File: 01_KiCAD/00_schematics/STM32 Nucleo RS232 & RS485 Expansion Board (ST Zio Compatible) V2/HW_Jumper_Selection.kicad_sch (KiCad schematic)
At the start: 0 parts

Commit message: Added components and change device
Added dual Schmidt trigger input SN74LVC2G14DBV for LED Rx and Tx control.
Changed sn74hcs245 for alternate part sn74lvc245a for larger footprint and better availability with LCSC.
Difference is sn74lvc245a has no Schmidt-trigger inputs but instead just normal inputs. Fot details see dataseet. Both devices use exact same pin number and configuration except sn74lvc245a has no thermal pad or exposed pad like the sn74hcs245 has.
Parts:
- added C27: 100nF, PCM_SparkFun-Capacitor:C_0603_1608Metric, symbol PCM_SparkFun-Capacitor:0.1uF_0603_25V_20%
- added D8, D9: LED, IN-S63AT:LED_0603_WRE, symbol PCM_SparkFun-LED:LED
- added J7: DIR, symbol Connector_Generic:Conn_01x03
- added R38: 590R, PCM_fab:R_0603, symbol PCM_fab:R_0603
- added R39: 137R, PCM_fab:R_0603, symbol PCM_fab:R_0603
- added R40, R41: 10K, PCM_fab:R_0603, symbol PCM_fab:R_0603
- added R42: 100K, PCM_fab:R_0603, symbol PCM_fab:R_0603
- added R43: 1M, PCM_fab:R_0603, symbol PCM_fab:R_0603
- added U5: SN74LVC2G14DBV, Package_TO_SOT_SMD:SOT-23-6, symbol 74xGxx:SN74LVC2G14DBV
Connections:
- new net: D8.2 (A), R39.1
- new net: D9.2 (A), R38.2
- new net: J7.1 (Pin_1), R40.2
- new net: J7.3 (Pin_3), R41.2
- new net: R42.2, U5.1 (1A)
- new net: D8.1 (K), U5.3 (2A), U5.6 (1Y)
- new net: D9.1 (K), U5.4 (2Y)
- new net 3V3_SYS: C27.1, R38.1, R39.2, R41.1, R43.2, U5.5 (V_{CC})
- new net DIR: J7.2 (Pin_2), R42.1, R43.1
- new net GND: C27.2, R40.1, U5.2 (GND)

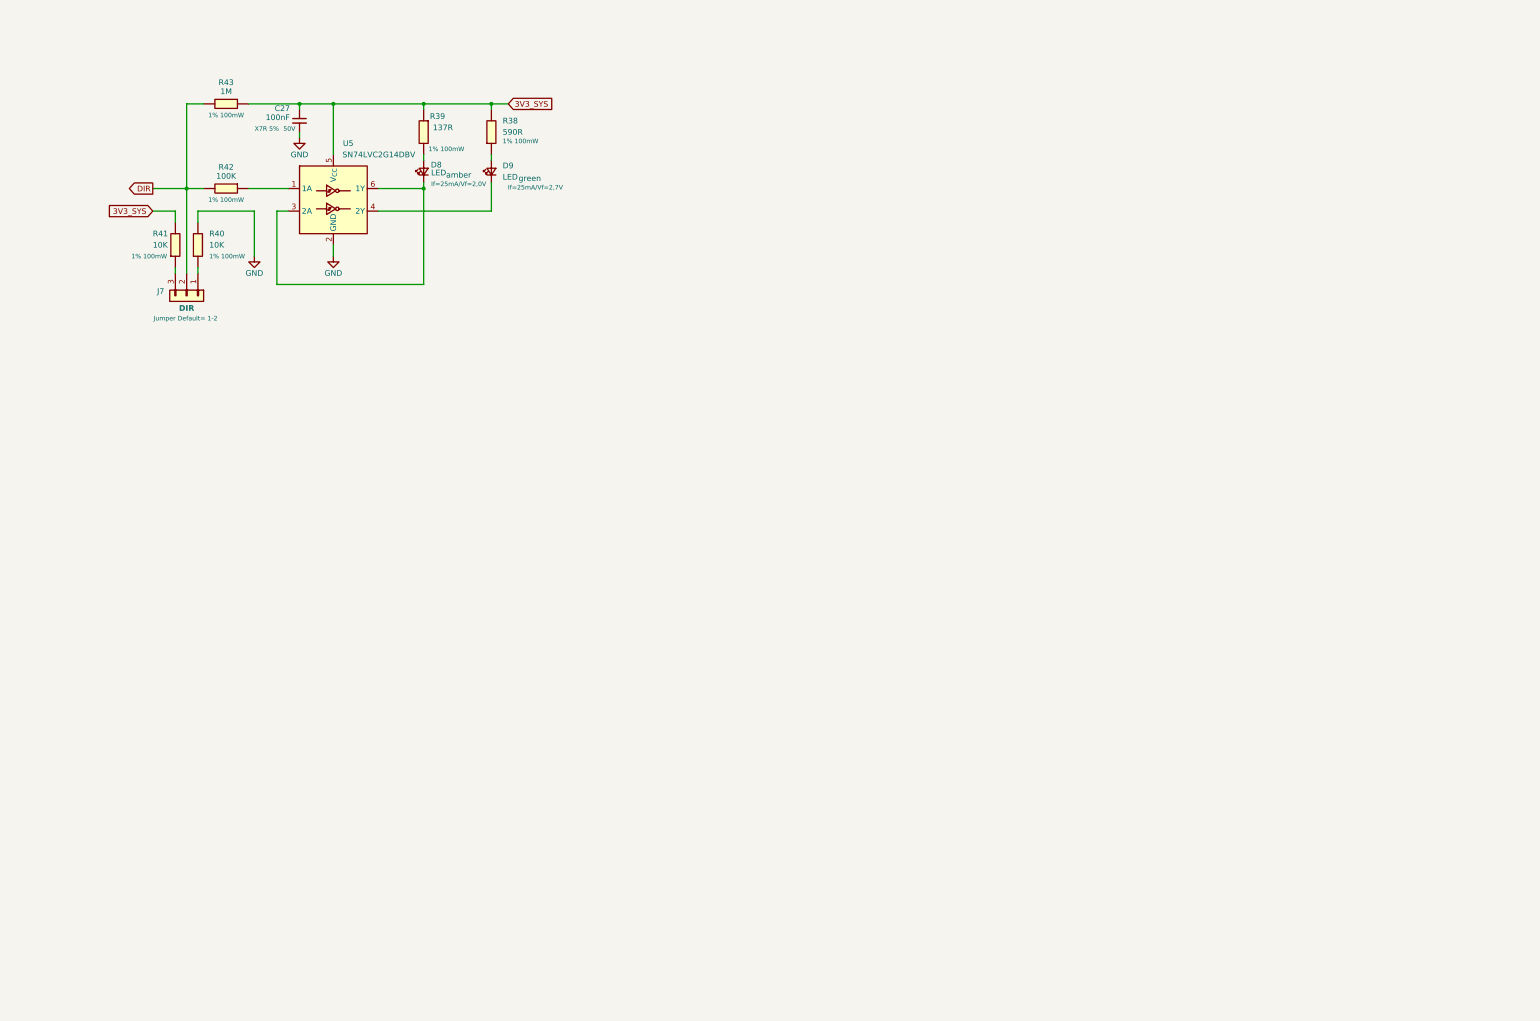
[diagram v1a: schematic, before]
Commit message: Finisching touches to schematics
Finalizing the schematics and double-check all connections throughout the different sheets.
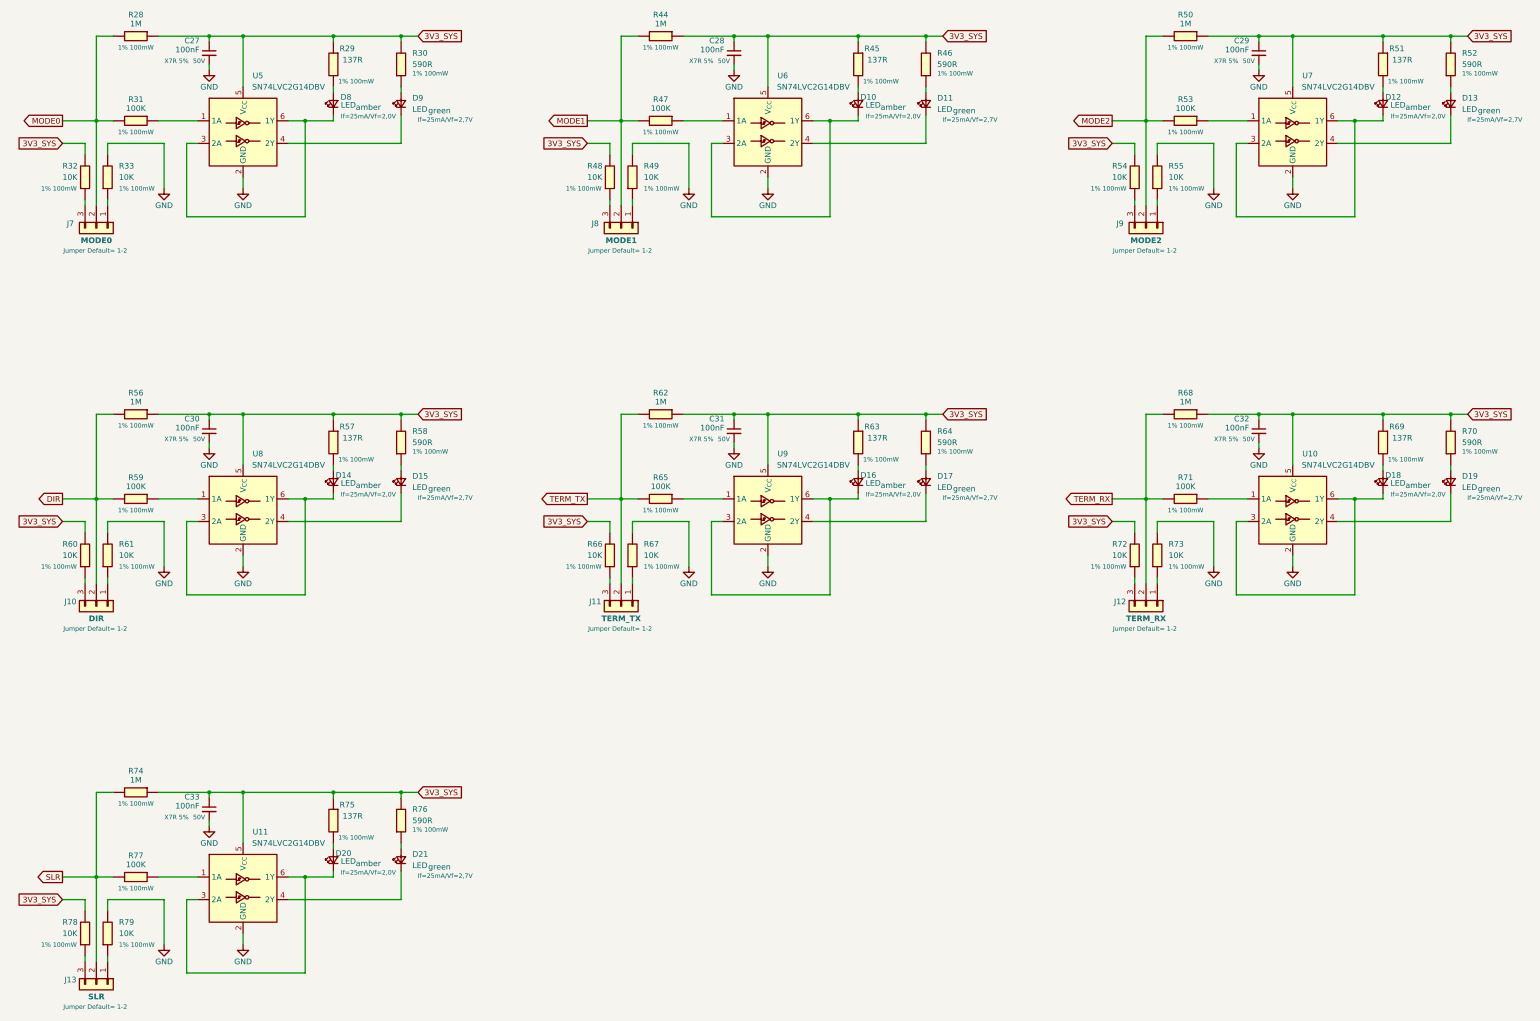
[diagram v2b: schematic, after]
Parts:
- added C28, C29, C30, C31, C32, C33: 100nF, PCM_SparkFun-Capacitor:C_0603_1608Metric, symbol PCM_SparkFun-Capacitor:0.1uF_0603_25V_20%
- added D10, D11, D12, D13, D14, D15, D16, D17, D18, D19, D20, D21: LED, IN-S63AT:LED_0603_WRE, symbol PCM_SparkFun-LED:LED
- added J10: DIR, symbol Connector_Generic:Conn_01x03
- added J11: TERM_TX, symbol Connector_Generic:Conn_01x03
- added J12: TERM_RX, symbol Connector_Generic:Conn_01x03
- added J13: SLR, symbol Connector_Generic:Conn_01x03
- added J8: MODE1, symbol Connector_Generic:Conn_01x03
- added J9: MODE2, symbol Connector_Generic:Conn_01x03
- added R44, R50, R56, R62, R68, R74: 1M, PCM_fab:R_0603, symbol PCM_fab:R_0603
- added R45, R51, R57, R63, R69, R75: 137R, PCM_fab:R_0603, symbol PCM_fab:R_0603
- added R46, R52, R58, R64, R70, R76: 590R, PCM_fab:R_0603, symbol PCM_fab:R_0603
- added R47, R53, R59, R65, R71, R77: 100K, PCM_fab:R_0603, symbol PCM_fab:R_0603
- added R48, R49, R54, R55, R60, R61, R66, R67, R72, R73, R78, R79: 10K, PCM_fab:R_0603, symbol PCM_fab:R_0603
- added U10, U11, U6, U7, U8, U9: SN74LVC2G14DBV, Package_TO_SOT_SMD:SOT-23-6, symbol 74xGxx:SN74LVC2G14DBV
- J7: value DIR -> MODE0
- renumbered R43 to R28, R39 to R29, R38 to R30, R42 to R31, R41 to R32, R40 to R33
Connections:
- net 3V3_SYS: now also C28.1, C29.1, C30.1, C31.1, C32.1, C33.1, R44.2, R45.2, R46.1, R48.1, R50.2, R51.2, R52.1, R54.1, R56.2, R57.2, R58.1, R60.1, R62.2, R63.2, R64.1, R66.1, R68.2, R69.2, R70.1, R72.1, R74.2, R75.2, R76.1, R78.1, U10.5 (V_{CC}), U11.5 (V_{CC}), U6.5 (V_{CC}), U7.5 (V_{CC}), U8.5 (V_{CC}), U9.5 (V_{CC})
- net DIR: now also J10.2 (Pin_2), R56.1, R59.1; no longer J7.2 (Pin_2), R28.1, R31.1
- net GND: now also C28.2, C29.2, C30.2, C31.2, C32.2, C33.2, R49.1, R55.1, R61.1, R67.1, R73.1, R79.1, U10.2 (GND), U11.2 (GND), U6.2 (GND), U7.2 (GND), U8.2 (GND), U9.2 (GND)
- new net: R59.2, U8.1 (1A)
- new net: D14.1 (K), U8.3 (2A), U8.6 (1Y)
- new net: D15.1 (K), U8.4 (2Y)
- new net: D13.2 (A), R52.2
- new net: J13.1 (Pin_1), R79.2
- new net: J10.3 (Pin_3), R60.2
- new net: J9.1 (Pin_1), R55.2
- new net: J9.3 (Pin_3), R54.2
- new net: J12.3 (Pin_3), R72.2
- new net: D21.2 (A), R76.2
- new net: R53.2, U7.1 (1A)
- new net: D12.1 (K), U7.3 (2A), U7.6 (1Y)
- new net: D13.1 (K), U7.4 (2Y)
- new net: D15.2 (A), R58.2
- new net: J11.1 (Pin_1), R67.2
- new net: J10.1 (Pin_1), R61.2
- new net: J11.3 (Pin_3), R66.2
- new net: R47.2, U6.1 (1A)
- new net: R77.2, U11.1 (1A)
- new net: D20.1 (K), U11.3 (2A), U11.6 (1Y)
- new net: D21.1 (K), U11.4 (2Y)
- new net: J8.1 (Pin_1), R49.2
- new net: J8.3 (Pin_3), R48.2
- new net: D17.1 (K), U9.4 (2Y)
- new net: D17.2 (A), R64.2
- new net: D12.2 (A), R51.1
- new net: J12.1 (Pin_1), R73.2
- new net: D20.2 (A), R75.1
- new net: R71.2, U10.1 (1A)
- new net: D16.1 (K), U9.3 (2A), U9.6 (1Y)
- new net: D16.2 (A), R63.1
- new net: R65.2, U9.1 (1A)
- new net: D14.2 (A), R57.1
- new net: D18.2 (A), R69.1
- new net: D11.2 (A), R46.2
- new net: D10.2 (A), R45.1
- new net: D19.2 (A), R70.2
- new net: D19.1 (K), U10.4 (2Y)
- new net: D10.1 (K), U6.3 (2A), U6.6 (1Y)
- new net: D11.1 (K), U6.4 (2Y)
- new net: D18.1 (K), U10.3 (2A), U10.6 (1Y)
- new net: J13.3 (Pin_3), R78.2
- new net MODE0: J7.2 (Pin_2), R28.1, R31.1
- new net MODE1: J8.2 (Pin_2), R44.1, R47.1
- new net MODE2: J9.2 (Pin_2), R50.1, R53.1
- new net SLR: J13.2 (Pin_2), R74.1, R77.1
- new net TERM_RX: J12.2 (Pin_2), R68.1, R71.1
- new net TERM_TX: J11.2 (Pin_2), R62.1, R65.1
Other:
- moved on the sheet: C27, D8, D9, J7, R28, R29, R30, R31, R32, R33, U5

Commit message: Finishing up the schematic aand created the board outline
Made some finishing touches to the schematic, updated all the symbol footprints and started to create the board.
Added missing 3D models for Phoenix 4-p RS485 connector and RS232 connector, also for Inolux LED.
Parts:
- J10, J11, J12, J13, J7, J8, J9: footprint (none) -> HTSW-103-07-F-S:CON3_1X3_TU_TSW
- renumbered R44 to R29, R50 to R30, R29 to R31, R30 to R32, R45 to R33, R46 to R34, R51 to R35, R52 to R36, R31 to R37, R47 to R38, R53 to R39, R32 to R40, R33 to R41, R48 to R42, R49 to R43, R54 to R44, R55 to R45, R56 to R46, R62 to R47, R68 to R48, R57 to R49, R58 to R50, R63 to R51, R64 to R52, R69 to R53, R70 to R54, R59 to R55, R65 to R56, R71 to R57, R60 to R58, R61 to R59, R66 to R60, R67 to R61, R72 to R62, R73 to R63, R74 to R64, R75 to R65, R76 to R66, R77 to R67, R78 to R68, R79 to R69

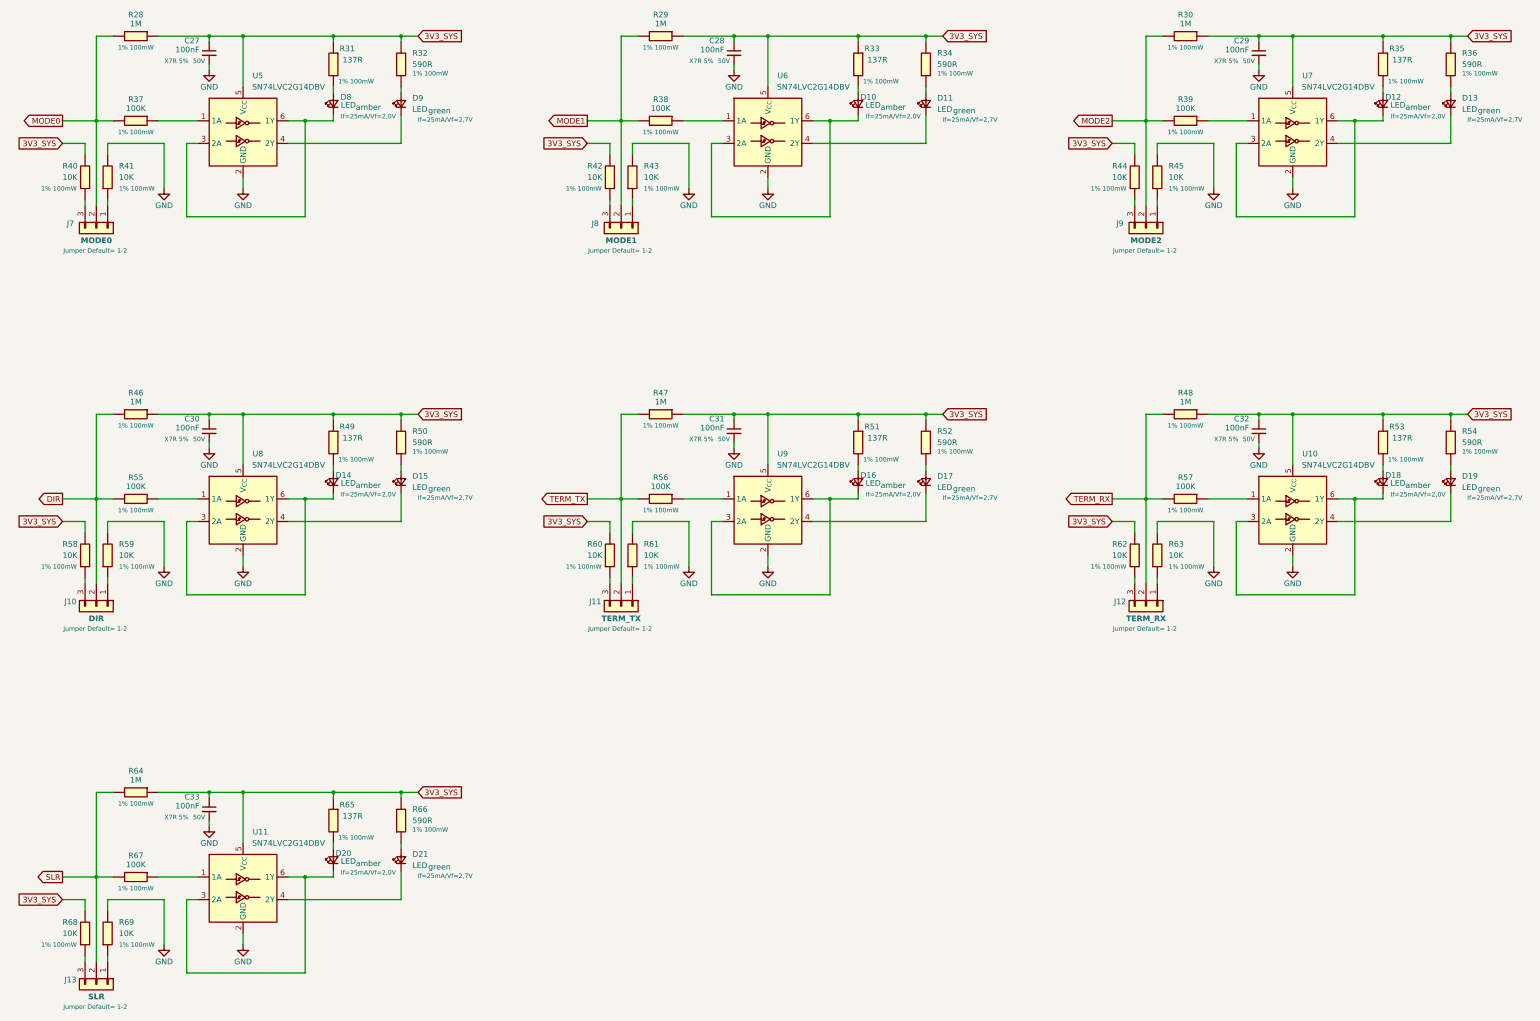
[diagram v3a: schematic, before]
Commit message: Updated footprints and added components to PCB
Added some additional components to the board. Changed the footprint of the 3-pin Jumper so the bottom silkscreen text doesnlt overlap with the Dual Schmidt Trigger IC's SN74LVC2G14
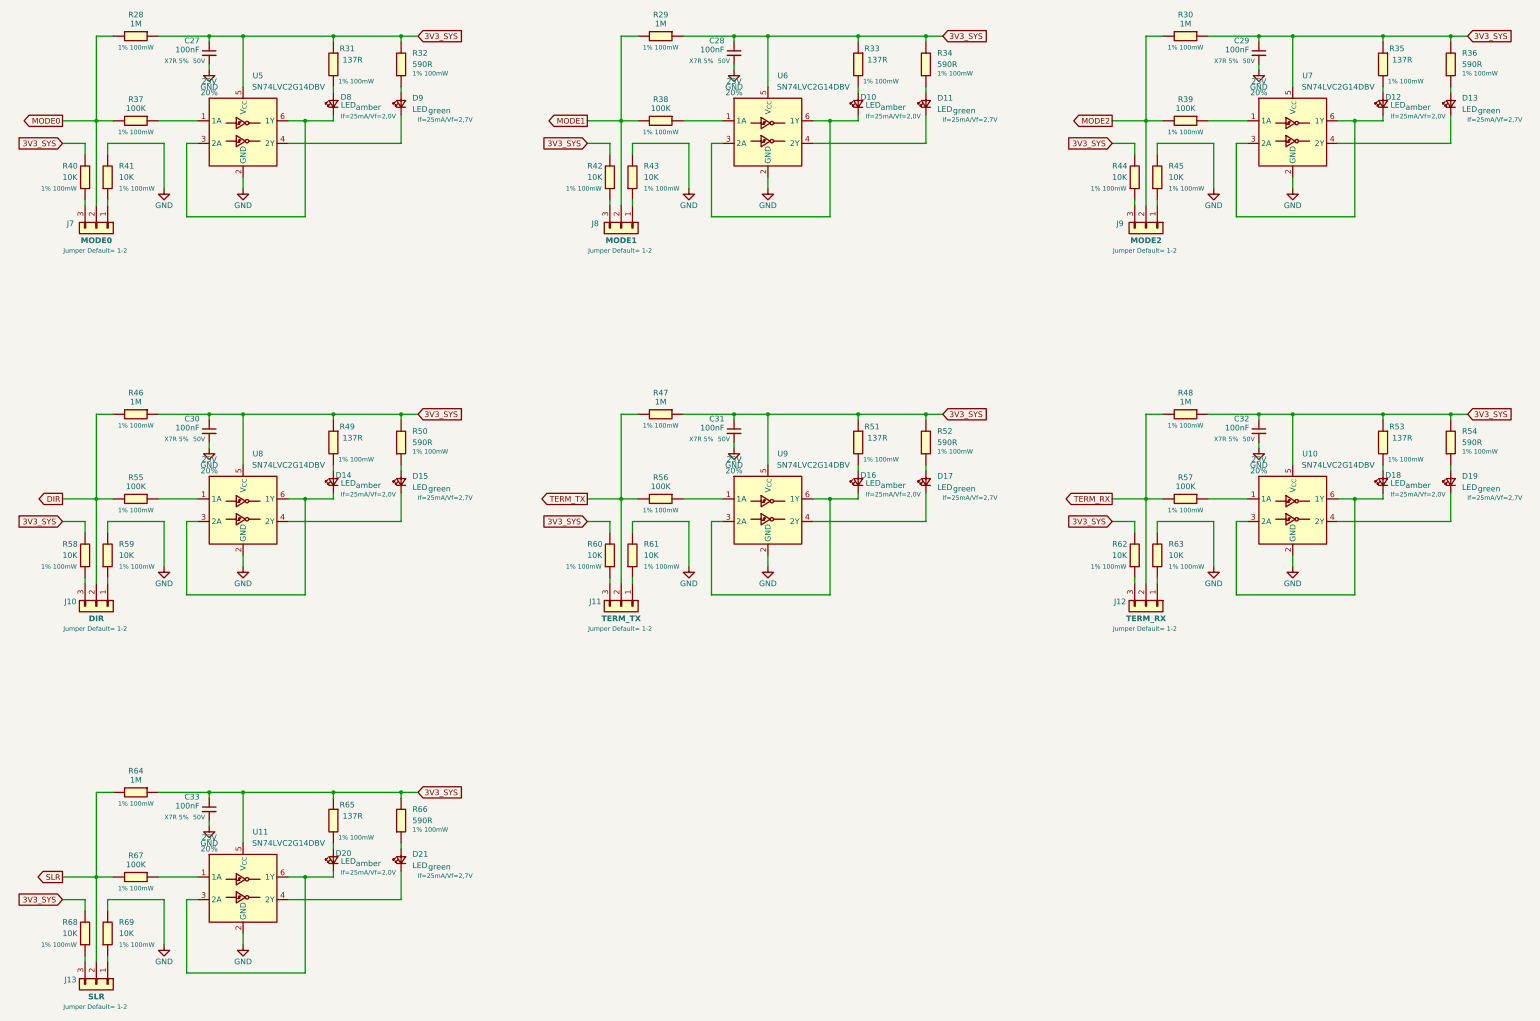
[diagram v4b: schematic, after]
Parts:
- C27, C28, C29, C30, C31, C32, C33: PROD_ID (none) -> CAP-00810; Tolerance (none) -> 20%; Voltage (none) -> 25V
- J10, J11, J12, J13, J7, J8, J9: footprint HTSW-103-07-F-S:CON3_1X3_TU_TSW -> Samtec_Connector:Samtec HTSW-103-07-F-S
